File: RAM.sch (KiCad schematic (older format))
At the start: 331 parts, among them J2 JTAG_01x06, J3 Conn_01x03_Male, U10 W25Q128JVS, U11 TPS62823DLC, U12 TPS62823DLC, U13 TPS62823DLC, U14 TPS62823DLC, U15 TPS62823DLC, U16 TPS62823DLC, U17 Si52112-B6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

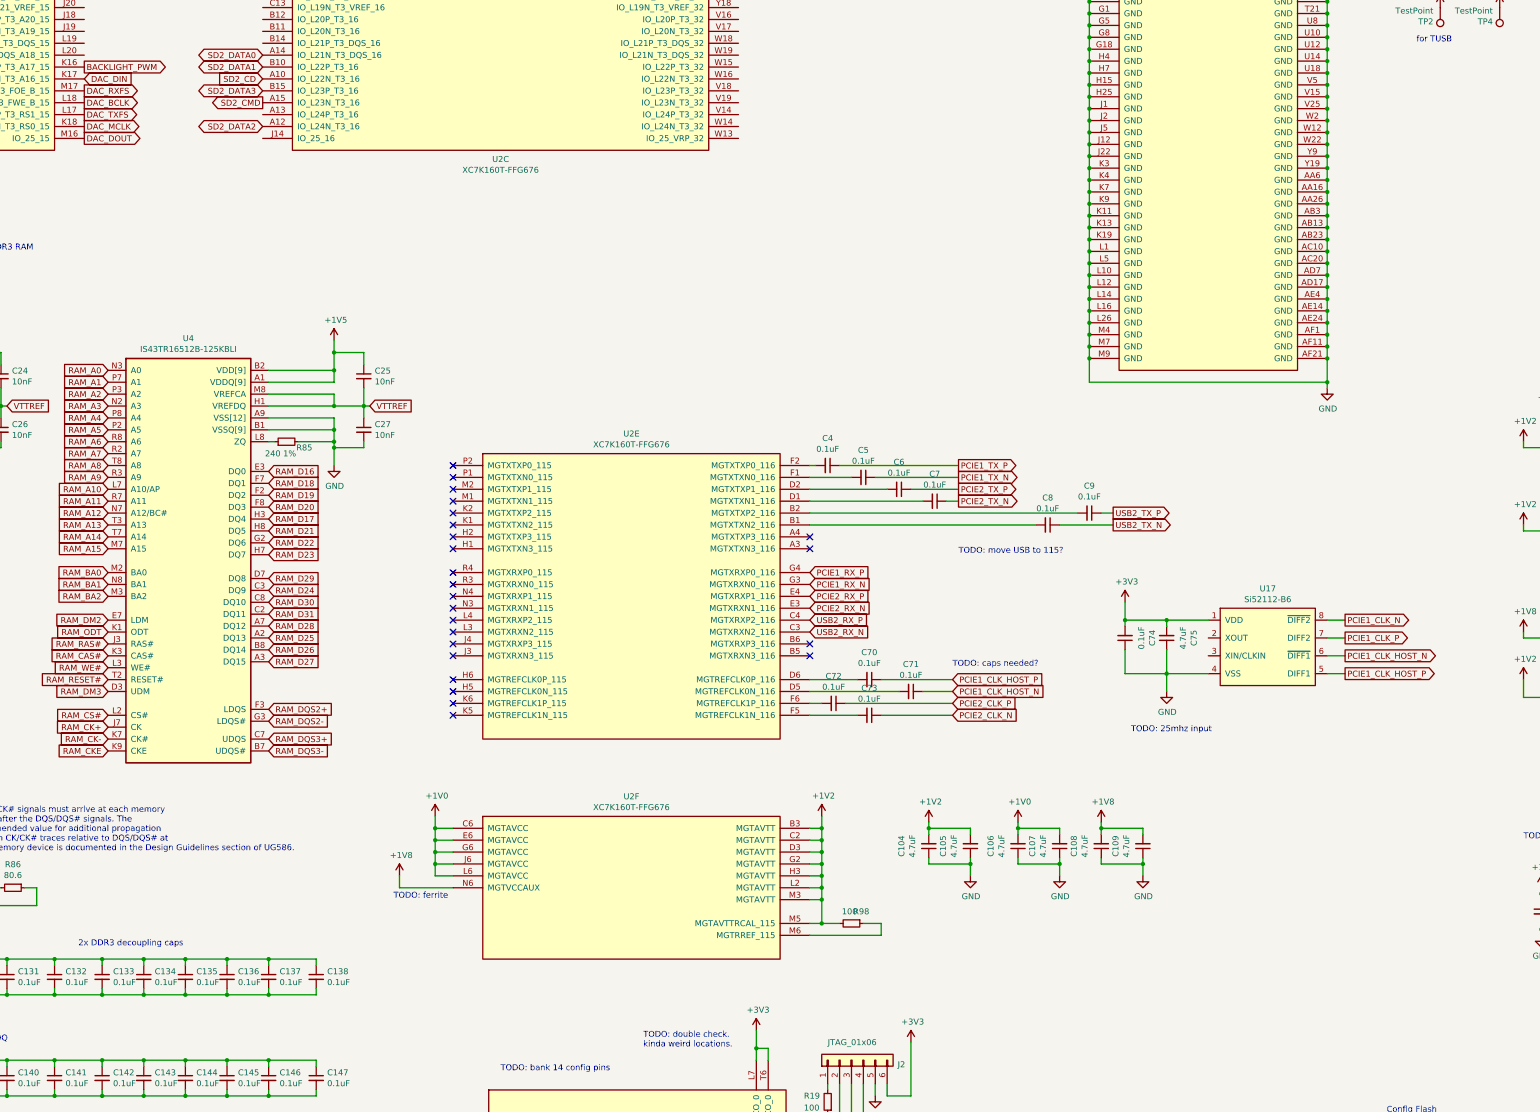
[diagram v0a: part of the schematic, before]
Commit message: more routing: 215 to go
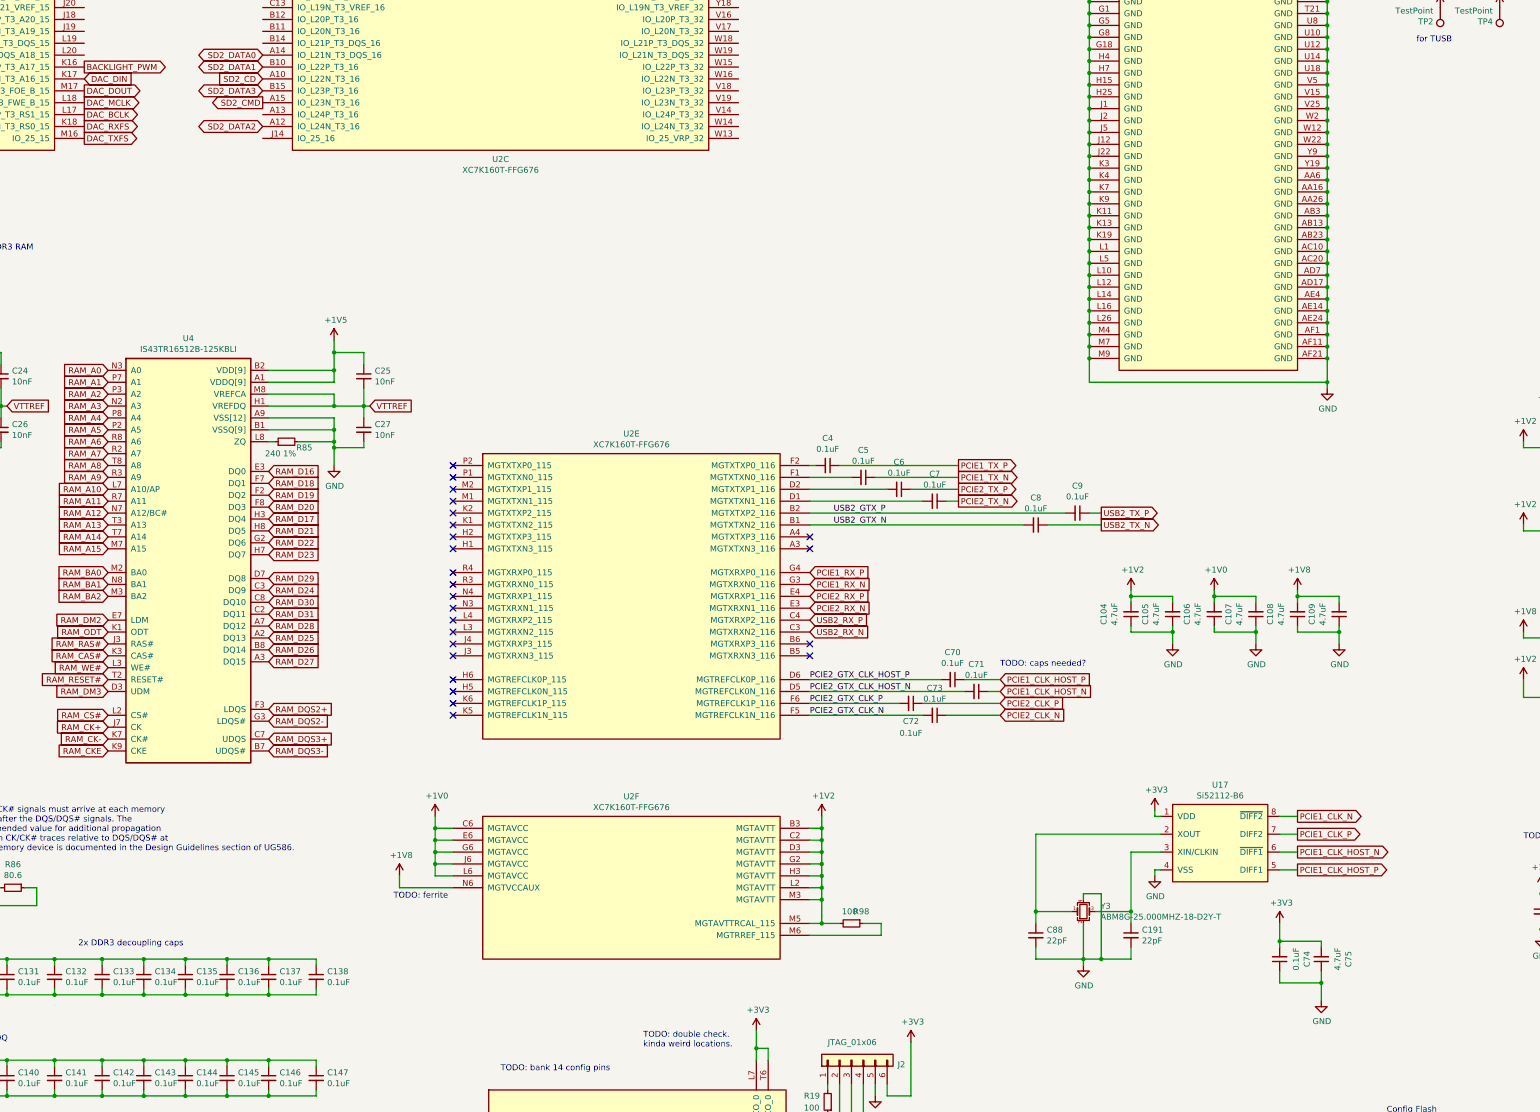
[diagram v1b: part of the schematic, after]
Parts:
- added C191, C88: 22pF, Capacitor_SMD:C_0402_1005Metric, symbol Device:C_Small
- added Y3: ABM8G-25.000MHZ-18-D2Y-T, Crystal:Crystal_SMD_3225-4Pin_3.2x2.5mm, symbol Device:Crystal_GND24_Small
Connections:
- net DAC_BCLK: now also U2.L17 (IO_L24P_T3_RS1_15); no longer U2.L18 (IO_L23N_T3_FWE_B_15)
- net DAC_DOUT: now also U2.M17 (IO_L23P_T3_FOE_B_15); no longer U2.M16 (IO_25_15)
- net DAC_MCLK: now also U2.L18 (IO_L23N_T3_FWE_B_15); no longer U2.K18 (IO_L24N_T3_RS0_15)
- net DAC_RXFS: now also U2.K18 (IO_L24N_T3_RS0_15); no longer U2.M17 (IO_L23P_T3_FOE_B_15)
- net DAC_TXFS: now also U2.M16 (IO_25_15); no longer U2.L17 (IO_L24P_T3_RS1_15)
- net GND: now also C191.2, C88.2, Y3.2, Y3.4
- net USB2_GTX_N: now reaches C8.2, U2.B1 (MGTXTXN2_116)
- net USB2_GTX_P: now reaches C9.2, U2.B2 (MGTXTXP2_116)
- net PCIE2_GTX_CLK_HOST_N: now reaches C71.2, U2.D5 (MGTREFCLK0N_116)
- net PCIE2_GTX_CLK_HOST_P: now reaches C70.2, U2.D6 (MGTREFCLK0P_116)
- net PCIE2_GTX_CLK_N: now reaches C73.2, U2.F5 (MGTREFCLK1N_116)
- net PCIE2_GTX_CLK_P: now reaches C72.2, U2.F6 (MGTREFCLK1P_116)
- net at U17.2 (XOUT): now also C88.1, Y3.1
- net at U17.3 (XIN/CLKIN): now also C191.1, Y3.3
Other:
- note removed: "TODO: 25mhz input"
- note removed: "TODO: move USB to 115?"
- moved on the sheet: C104, C105, C106, C107, C108, C109, C70, C71, C72, C73, C74, C75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

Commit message: add power sequencer, main clock, some missing resets, more routing (198)
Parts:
- added C192: 0.1uF, Capacitor_SMD:C_0402_1005Metric, symbol Device:C_Small
- added R100, R99: 80.6, Resistor_SMD:R_0402_1005Metric, symbol Device:R_Small
- added R101: 0, Resistor_SMD:R_0603_1608Metric, symbol Device:R_Small
- added TP13: TestPoint, TestPoint:TestPoint_Pad_1.0x1.0mm, symbol Connector:TestPoint
- added U18: LM3880, Package_TO_SOT_SMD:SOT-23-6, symbol Power_Supervisor:LM3880
- added X1: ASFLMB-100.000MHZ-XY-T, Oscillator:Oscillator_SMD_Abracon_ASE-4Pin_3.2x2.5mm, symbol Oscillator:ASE-xxxMHz
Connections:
- net +1V5: now also R99.2
- net +3V3: now also C192.1, X1.1 (EN), X1.4 (Vdd)
- net +5V: now also U12.1 (EN), R101.1, U18.1 (VCC)
- net DISP1_SCL: now also U2.G12 (IO_L16P_T2_16)
- net DISP1_SDA: now also U2.A13 (IO_L24P_T3_16)
- net DSI_RST_N: now also U2.AB26 (IO_L9P_T1_DQS_12)
- net GND: now also C192.2, R100.1, U18.2 (GND), X1.2 (GND)
- net HDMI_RST_N: now also U2.C13 (IO_L19N_T3_VREF_16)
- net I2C1_SCL: now also U2.G26 (IO_L16N_T2_A15_D31_14)
- net I2C1_SDA: now also U2.H26 (IO_L18N_T2_A11_D27_14)
- net PCIE1_RESETn: now reaches U2.A17 (IO_L3N_T0_DQS_AD1N_15)
- net PCIE2_RESETn: now reaches U2.A18 (IO_L2P_T0_AD8P_15)
- net CLK_100MHZ: now reaches U2.F22 (IO_L12P_T1_MRCC_14)
- net CLK_100MHZ: now also TP13.1, X1.3 (OUT)
- net at U2.U4 (IO_0_VRN_34): now also R99.1
- net at U2.V12 (IO_25_VRP_33): now also R100.2
- net EN_VIO: now reaches U11.1 (EN)
- net EN_VIO: now also U13.1 (EN), U16.1 (EN), U18.4 (FLAG3)
- net EN_VDDR: now reaches U5.7 (EN)
- net EN_VDDR: now also U14.1 (EN), U18.5 (FLAG2)
- net EN_VAUX: now reaches U15.1 (EN)
- net EN_VAUX: now also U18.6 (FLAG1)
- new net: R101.2, U18.3 (EN)
- no-connect marks 48 -> 58
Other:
- note added: "DCI resistors"
- note added: "MAIN CLOCK (100MHz)"
- note added: "See AR# 41590"
- note added: "TODO: can i use this?"
- note removed: "TODO: enables? power sequencing?"
- note removed: "TODO: floorplan"
- note removed: "TODO: why?"
- note removed: "antmicro use ASFLMB-100.000MHZ-XY-T"
- moved on the sheet: C101, C102, C103, C117, C13, C14, C189, C190, C67, C69, C76, C78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

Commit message: fully routed
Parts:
- removed R71: 0, Resistor_SMD:R_0402_1005Metric, symbol Device:R_Small
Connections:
- net TUSB_CLKOUT: now also U2.Y23 (IO_L12P_T1_MRCC_12), U7.D10 (CLKOUT)
- net UART3_RX: now also U2.G16 (IO_L7N_T1_AD10N_15); no longer U2.H16 (IO_L7P_T1_AD10P_15)
- net UART3_TX: now also U2.H16 (IO_L7P_T1_AD10P_15); no longer U2.G16 (IO_L7N_T1_AD10N_15)
- no-connect marks 58 -> 75
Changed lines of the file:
@@
 Text GLabel 12800 6500 0    50   Input ~ 0
 SD2_CD
-Text GLabel 11300 3400 2    50   Input ~ 0
+Text GLabel 11300 3500 2    50   Input ~ 0
 UART3_RX
-Text GLabel 11300 3500 2    50   Output ~ 0
+Text GLabel 11300 3400 2    50   Output ~ 0
 UART3_TX
 $Comp
@@
 Wire Wire Line
 	8700 20550 8700 20950
-Wire Wire Line
-	8700 20950 9100 20950
-$Comp
-L Device:R_Small R71
-U 1 1 6201CD91
-P 9200 20950
-F 0 "R71" V 9250 20800 50  0000 C CNN
-F 1 "0" V 9250 21150 50  0000 C CNN
-F 2 "Resistor_SMD:R_0402_1005Metric" H 9200 20950 50  0001 C CNN
-F 3 "~" H 9200 20950 50  0001 C CNN
-	1    9200 20950
-	0    -1   1    0
-$EndComp
 Text GLabel 9500 20950 2    50   Output ~ 0
 TUSB_CLKOUT
-Wire Wire Line
-	9500 20950 9300 20950
 $Comp
 L Device:R_Small R59
@@
 Text GLabel 11300 2400 2    50   Output ~ 0
 PCIE2_RESETn
+NoConn ~ 11300 3300
+NoConn ~ 11300 3600
+NoConn ~ 11300 2900
+NoConn ~ 11300 2800
+NoConn ~ 11300 2600
+NoConn ~ 11300 2500
+NoConn ~ 11300 2300
+NoConn ~ 11300 6300
+NoConn ~ 11300 6200
+NoConn ~ 11300 6100
+NoConn ~ 11300 6000
+NoConn ~ 11300 5900
+NoConn ~ 11300 5800
+NoConn ~ 11300 5700
+NoConn ~ 11300 5600
+NoConn ~ 11300 5500
+NoConn ~ 11300 5400
+Text GLabel 1500 4400 0    50   Input ~ 0
+TUSB_CLKOUT
+Wire Wire Line
+	8700 20950 9500 20950
 $EndSCHEMATC

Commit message: connect some missing i2c signals, backlight_en
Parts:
- added R102, R103, R104, R71: 4k7, Resistor_SMD:R_0402_1005Metric, symbol Device:R_Small
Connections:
- net +1V8: now also R102.1, R103.1, R104.1, R71.1
- net DISP1_SCL: now also R102.2
- net DISP1_SDA: now also R71.2
- net DISP2_SDA: now reaches U2.W26 (IO_L5N_T0_12)
- net DISP2_SDA: now also U8.B8 (I2C_SDA), R103.2
- net DISP2_SCL: now reaches U2.Y26 (IO_L10N_T1_12)
- net DISP2_SCL: now also U8.A8 (I2C_SCL), R104.2
- net BACKLIGHT_EN: now reaches U2.B16 (IO_L1N_T0_AD0N_15)
- net DSI_REFCLK: now reaches U8.K6 (REFCLK)
- net I2C1_SCL renamed DAC_SDA
- net DAC_SDA: no longer U8.A8 (I2C_SCL)
- net I2C1_SDA renamed DAC_SCL
- net DAC_SCL: no longer U8.B8 (I2C_SDA)
- no-connect marks 75 -> 77
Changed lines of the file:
@@
 Wire Wire Line
 	32200 12700 32450 12700
-Text GLabel 30050 9550 0    50   BiDi ~ 0
-I2C1_SDA
-Text GLabel 30050 9650 0    50   Input ~ 0
-I2C1_SCL
 Text GLabel 30050 9150 0    50   Input ~ 0
 DSI_RST_N
@@
 NoConn ~ 18800 10650
 NoConn ~ 18800 10750
-Text GLabel 7300 5300 0    50   Output ~ 0
-I2C1_SCL
+Text GLabel 7300 5700 0    50   Output ~ 0
+DAC_SCL
 Text GLabel 12800 5200 0    50   Output ~ 0
 DISP1_SCL
 Text GLabel 12800 6800 0    50   BiDi ~ 0
 DISP1_SDA
-Text GLabel 7300 5700 0    50   BiDi ~ 0
-I2C1_SDA
+Text GLabel 7300 5300 0    50   BiDi ~ 0
+DAC_SDA
 Text GLabel 11300 2700 2    50   Output ~ 0
 PCIE1_RESETn
@@
 NoConn ~ 11300 2600
 NoConn ~ 11300 2500
-NoConn ~ 11300 2300
 NoConn ~ 11300 6300
 NoConn ~ 11300 6200
@@
 Wire Wire Line
 	8700 20950 9500 20950
+NoConn ~ 6050 10700
+NoConn ~ 2050 12200
+NoConn ~ 2050 12100
+Text GLabel 30050 9250 0    50   Input ~ 0
+DSI_REFCLK
+Wire Wire Line
+	30050 9250 30200 9250
+Text GLabel 30050 9650 0    50   Input ~ 0
+DISP2_SCL
+Text GLabel 30050 9550 0    50   BiDi ~ 0
+DISP2_SDA
+Text GLabel 1500 4100 0    50   Output ~ 0
+DISP2_SCL
+Text GLabel 1500 3100 0    50   BiDi ~ 0
+DISP2_SDA
+$Comp
+L Device:R_Small R103
+U 1 1 86B879B1
+P 30350 15000
+F 0 "R103" H 30409 15046 50  0000 L CNN
+F 1 "4k7" H 30409 14955 50  0000 L CNN
+F 2 "Resistor_SMD:R_0402_1005Metric" H 30350 15000 50  0001 C CNN
+F 3 "~" H 30350 15000 50  0001 C CNN
+	1    30350 15000
+	1    0    0    -1
+$EndComp
+$Comp
+L Device:R_Small R104
+U 1 1 86B88850
+P 31050 15000
+F 0 "R104" H 31109 15046 50  0000 L CNN
+F 1 "4k7" H 31109 14955 50  0000 L CNN
+F 2 "Resistor_SMD:R_0402_1005Metric" H 31050 15000 50  0001 C CNN
+F 3 "~" H 31050 15000 50  0001 C CNN
+	1    31050 15000
+	1    0    0    -1
+$EndComp
+Text GLabel 30200 15200 0    50   BiDi ~ 0
+DISP2_SDA
+Wire Wire Line
+	30200 15200 30350 15200
+Wire Wire Line
+	30350 15200 30350 15100
+Text GLabel 30950 15200 0    50   Input ~ 0
+DISP2_SCL
+Wire Wire Line
+	30950 15200 31050 15200
+Wire Wire Line
+	31050 15200 31050 15100
+$Comp
+L power:+1V8 #PWR0193
+U 1 1 876B8409
+P 30350 14750
+F 0 "#PWR0193" H 30350 14600 50  0001 C CNN
+F 1 "+1V8" H 30365 14923 50  0000 C CNN
+F 2 "" H 30350 14750 50  0001 C CNN
+F 3 "" H 30350 14750 50  0001 C CNN
+	1    30350 14750
+	1    0    0    -1
+$EndComp
+Wire Wire Line
+	30350 14750 30350 14850
+Wire Wire Line
+	30350 14850 31050 14850
+Wire Wire Line
+	31050 14850 31050 14900
+Connection ~ 30350 14850
+Wire Wire Line
+	30350 14850 30350 14900
+$Comp
+L Device:R_Small R71
+U 1 1 87E393A2
+P 25100 14350
+F 0 "R71" H 25159 14396 50  0000 L CNN
+F 1 "4k7" H 25159 14305 50  0000 L CNN
+F 2 "Resistor_SMD:R_0402_1005Metric" H 25100 14350 50  0001 C CNN
+F 3 "~" H 25100 14350 50  0001 C CNN
+	1    25100 14350
+	1    0    0    -1
+$EndComp
+$Comp
+L Device:R_Small R102
+U 1 1 87E3EB80
+P 25800 14350
+F 0 "R102" H 25859 14396 50  0000 L CNN
+F 1 "4k7" H 25859 14305 50  0000 L CNN
+F 2 "Resistor_SMD:R_0402_1005Metric" H 25800 14350 50  0001 C CNN
+F 3 "~" H 25800 14350 50  0001 C CNN
+	1    25800 14350
+	1    0    0    -1
+$EndComp
+Text GLabel 24950 14550 0    50   BiDi ~ 0
+DISP1_SDA
+Wire Wire Line
+	24950 14550 25100 14550
+Wire Wire Line
+	25100 14550 25100 14450
+Text GLabel 25700 14550 0    50   Input ~ 0
+DISP1_SCL
+Wire Wire Line
+	25700 14550 25800 14550
+Wire Wire Line
+	25800 14550 25800 14450
+$Comp
+L power:+1V8 #PWR0194
+U 1 1 87E3EB90
+P 25100 14100
+F 0 "#PWR0194" H 25100 13950 50  0001 C CNN
+F 1 "+1V8" H 25115 14273 50  0000 C CNN
+F 2 "" H 25100 14100 50  0001 C CNN
+F 3 "" H 25100 14100 50  0001 C CNN
+	1    25100 14100
+	1    0    0    -1
+$EndComp
+Wire Wire Line
+	25100 14100 25100 14200
+Wire Wire Line
+	25100 14200 25800 14200
+Wire Wire Line
+	25800 14200 25800 14250
+Connection ~ 25100 14200
+Wire Wire Line
+	25100 14200 25100 14250
+Text GLabel 11300 2300 2    50   Output ~ 0
+BACKLIGHT_EN
 $EndSCHEMATC
